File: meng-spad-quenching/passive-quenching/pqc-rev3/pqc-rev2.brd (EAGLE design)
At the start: 38.1 x 25.4 mm, 62 parts, among them IC1 OPA858, IC2 OPA858, IC3 NUD3160DMT1G, IC4 TPS7A4901, X1 CONN_SPAD, X2 VIN_PWR, X4 VIN_BIAS, X5 SIGNAL_OUT

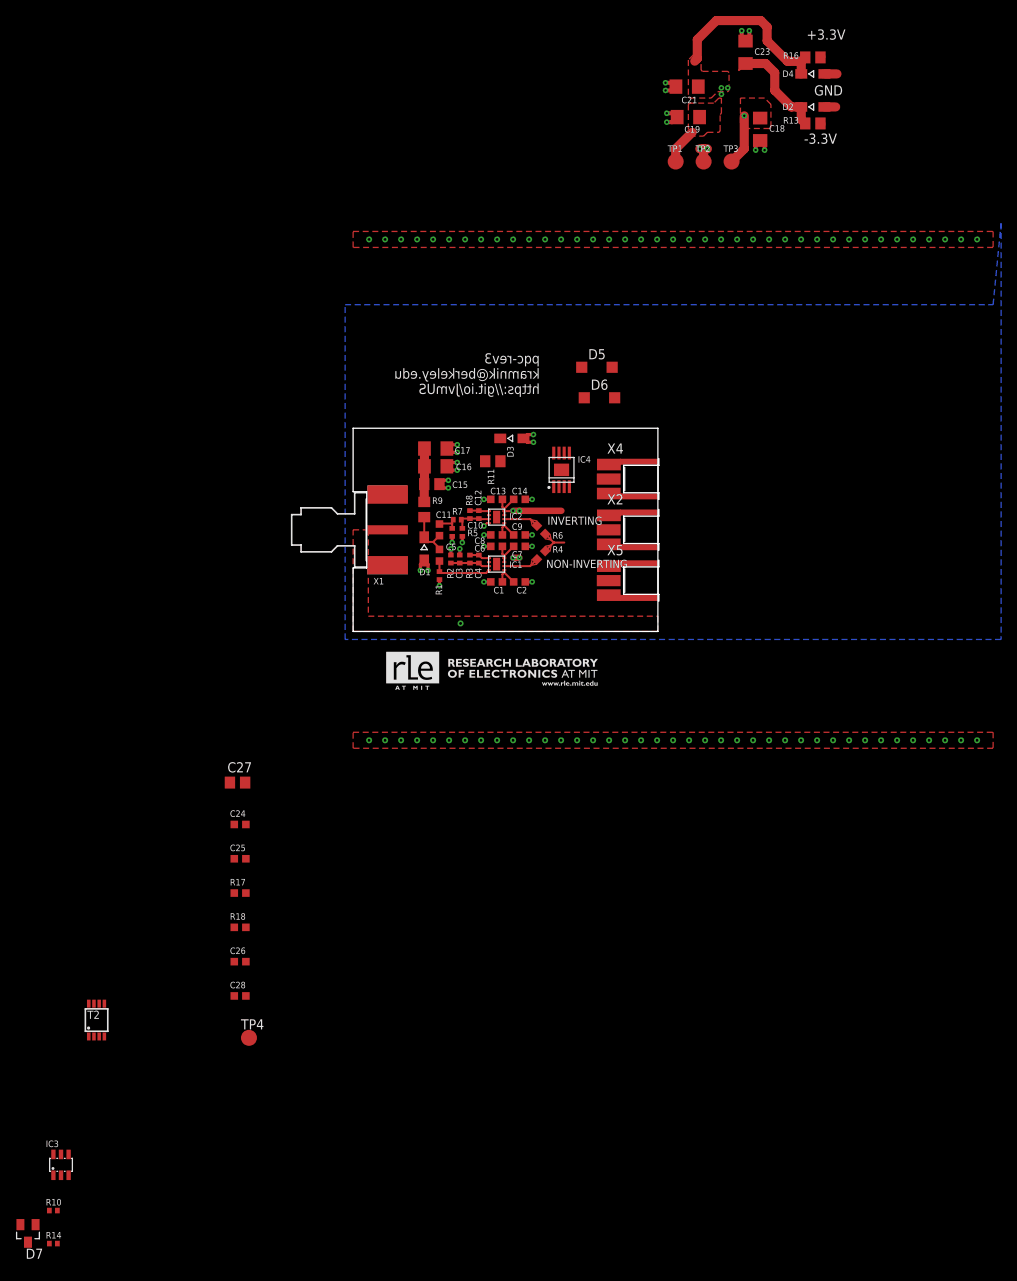
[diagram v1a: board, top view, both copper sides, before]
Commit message: 2 different power supply switching options investigated in sim
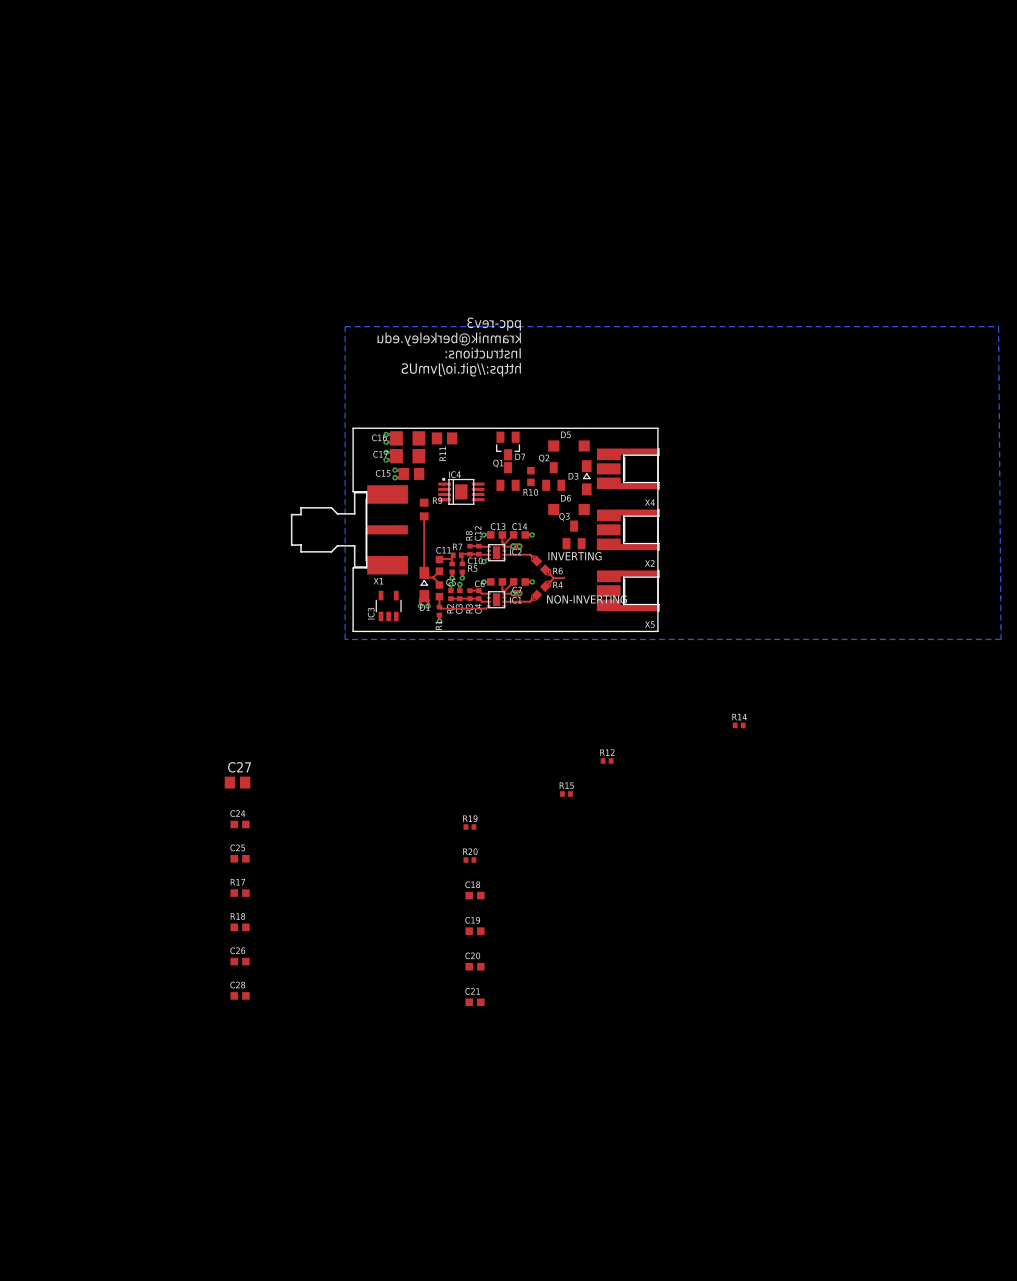
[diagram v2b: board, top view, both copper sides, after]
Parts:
- removed C1, C8: CAP CER 10000PF 25V C0G 0603, rcl-modified-footprints:C0603
- removed C2, C9: CAP CER 0.1UF 25V X7R 0603, rcl-modified-footprints:C0603
- removed C23: CAP CER 10UF 16V X7R 1206, rcl:C1206
- removed D2, D4: DF2B36FU,H3F, diode:SOD323-W
- removed R13, R16: RES SMD 1 OHM 1% 0805, rcl-modified-footprints:R0805
- removed T2: (no value), zetex:MSOP8
- removed TP1: P2V5, testpad:TP20R
- removed TP2, TP4: GND, testpad:TP20R
- removed TP3: N2V5, testpad:TP20R
- added C20: CAP CER 0.1UF 100V X7R 0603, rcl-modified-footprints:C0603
- added Q1: NTR5105P, meng:SOT23C
- added Q2: BSS123LT1G, meng:SOT23C
- added Q3: NUD3160LT1G, meng:SOT23C
- added R12: RES SMD 10M OHM 1% 1/10W 0603, rcl-modified-footprints:R0402
- added R15: RES SMD 10K OHM 1% 1/10W 0603, rcl-modified-footprints:R0402
- added R19, R20: RES SMD 1K OHM 1% 1/10W 0603, rcl-modified-footprints:R0402
- C18, C19, C21: value CAP CER 10UF 16V X7R 1206 -> CAP CER 0.1UF 100V X7R 0603; device rcl:C1206 -> rcl-modified-footprints:C0603
- C28: value CAP CER 0.1UF 25V X7R 0603 10% -> CAP CER 0.1UF 100V X7R 0603
- IC3: value NUD3160DMT1G -> LM8261; device meng:SOT23-6L -> meng:SOT23-5
- R10: value RES SMD 33K OHM 1% 1/10W 0603 -> RES SMD 10M OHM 1% 1/10W 0603; device rcl-modified-footprints:R0402 -> rcl-modified-footprints:R0603
- R14: value RES SMD 33K OHM 1% 1/10W 0603 -> RES SMD 10K OHM 1% 1/10W 0603
- R9: device rcl:R0805 -> rcl:R0603
- moved C21 117.5 mm to (15.2, -46.4), turned to 0 degrees
- moved D7 115.3 mm to (19.4, 23.2)
- moved R10 109.5 mm to (22.2, 19.4), turned to 90 degrees
- moved R14 107.4 mm to (48.3, -11.7)
- moved C19 105.2 mm to (15.2, -37.5), turned to 0 degrees
- moved C18 102.2 mm to (15.2, -33.0), turned to 0 degrees
- moved IC3 81.0 mm to (4.45, 3.17)
- moved D6 14.5 mm to (27.0, 15.2)
- moved IC4 13.7 mm to (11.4, 18.4), turned to 270 degrees
- moved D3 10.6 mm to (29.2, 19.2), turned to 270 degrees
- moved D5 10.4 mm to (27.0, 23.2)
- moved R11 6.68 mm to (11.4, 24.1)
- moved C16 4.94 mm to (6.83, 24.1), turned to 180 degrees
- moved C13 4.45 mm to (17.9, 12.1)
- moved C14 4.45 mm to (20.8, 12.1)
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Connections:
- removed net N$14: D6.A, IC3.2, X2.1
- removed net N$15: IC3.4, R14.2
- removed net N$9: IC3.5, IC3.6, R10.1
- removed net PP_N2V5_ANALOG: C1.1, C18.1, C2.1, C8.1, C9.1, TP3.TP
- removed net PP_NVIN: C23.1, D2.C, R13.1
- removed net PP_NVIN_CONN: R13.2
- removed net PP_P15V0_ANALOG: C28.1, D6.C, IC4.5, IC4.8, T2.5, T2.6
- removed net PP_P2V5_ANALOG: C19.1, TP1.TP
- removed net PP_PVIN: C21.1, D4.C, R16.1
- removed net PP_PVIN_CONN: R16.2
- new net LDO_IN: C28.1, D6.C, IC4.5, IC4.8, Q1.3
- new net LOAD_SW_NMOS_DRAIN: Q2.3, R15.1
- new net LOAD_SW_NMOS_GATE: Q2.1, Q3.3, R10.1
- new net LOAD_SW_NMOS_SOURCE: Q2.2, R14.2
- new net N$17: C18.1, IC3.3, R19.1, R20.2
- new net VPWR_IN: D6.A, Q3.1, X2.1
- new net VREF_2V5: C10.2, C20.1, C21.1, C3.2, IC3.1, IC3.4, R1.1, R2.2, R5.1
- net GND: now also C20.2, IC3.2, Q3.2, R20.1; no longer C1.2, C10.2, C2.2, C23.2, C3.2, C8.2, C9.2, D2.A, D4.A, IC3.1, R1.1, R2.2, R5.1, TP2.TP
- net LOAD_SW_PMOS_GATE: now also Q1.1, R12.1, R15.2; no longer IC3.3, T2.4
- net LOAD_SW_PMOS_SOURCE: now also Q1.2, R12.2; no longer T2.3
- net PP_P5V0_ANALOG: now also C19.1, IC3.5, R19.2; no longer TP4.TP
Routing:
- net GND: track 44.0 -> 16.1 mm, vias 116 -> 13
- net PP_PVIN: track 22.2 -> 0.00 mm
- net PP_NVIN: track 14.0 -> 0.00 mm
- net PP_N2V5_ANALOG: track 12.3 -> 0.00 mm, vias 1 -> 0
- net N$1: track 6.72 -> 0.00 mm
- net N$2: track 6.61 -> 11.2 mm
- net PP_P2V5_ANALOG: track 4.51 -> 0.00 mm
- net PP_P5V0_ANALOG: track 24.0 -> 19.8 mm
- net VREF_2V5: track 0.00 -> 3.85 mm, vias 0 -> 5
- removed copper zone on layer 1, net GND
- removed copper zone on layer 1, net PP_N2V5_ANALOG
- removed copper zone on layer 1, net PP_P2V5_ANALOG
- removed copper zone on layer 1, net PP_PVIN
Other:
- board text added: "pqc-rev3 kramnik@berkeley.edu Instructions: https://git.io/JvmUS"
- board text removed: "+3.3V"
- board text removed: "-3.3V"
- board text removed: "GND"
- board text removed: "pqc-rev3 kramnik@berkeley.edu https://git.io/JvmUS"

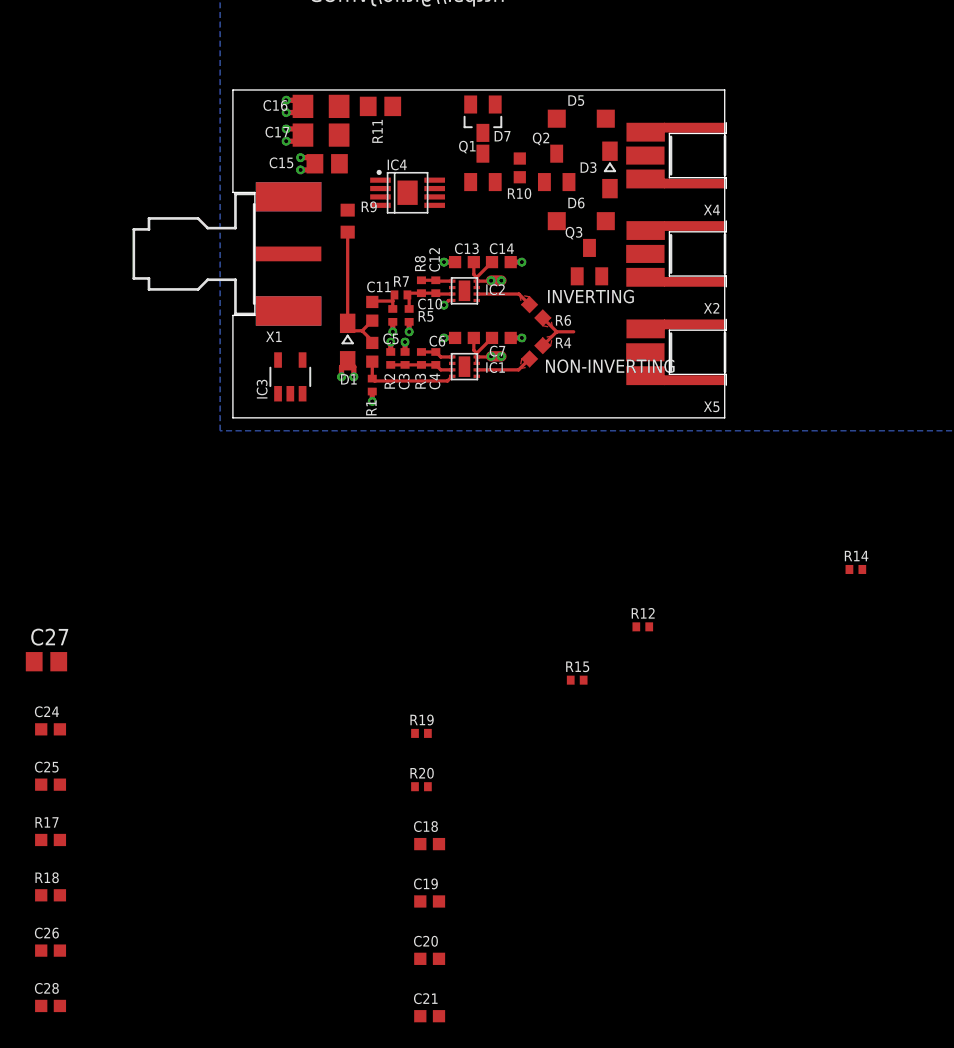
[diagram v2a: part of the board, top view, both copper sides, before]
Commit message: Everything fits on board, placement still preliminary
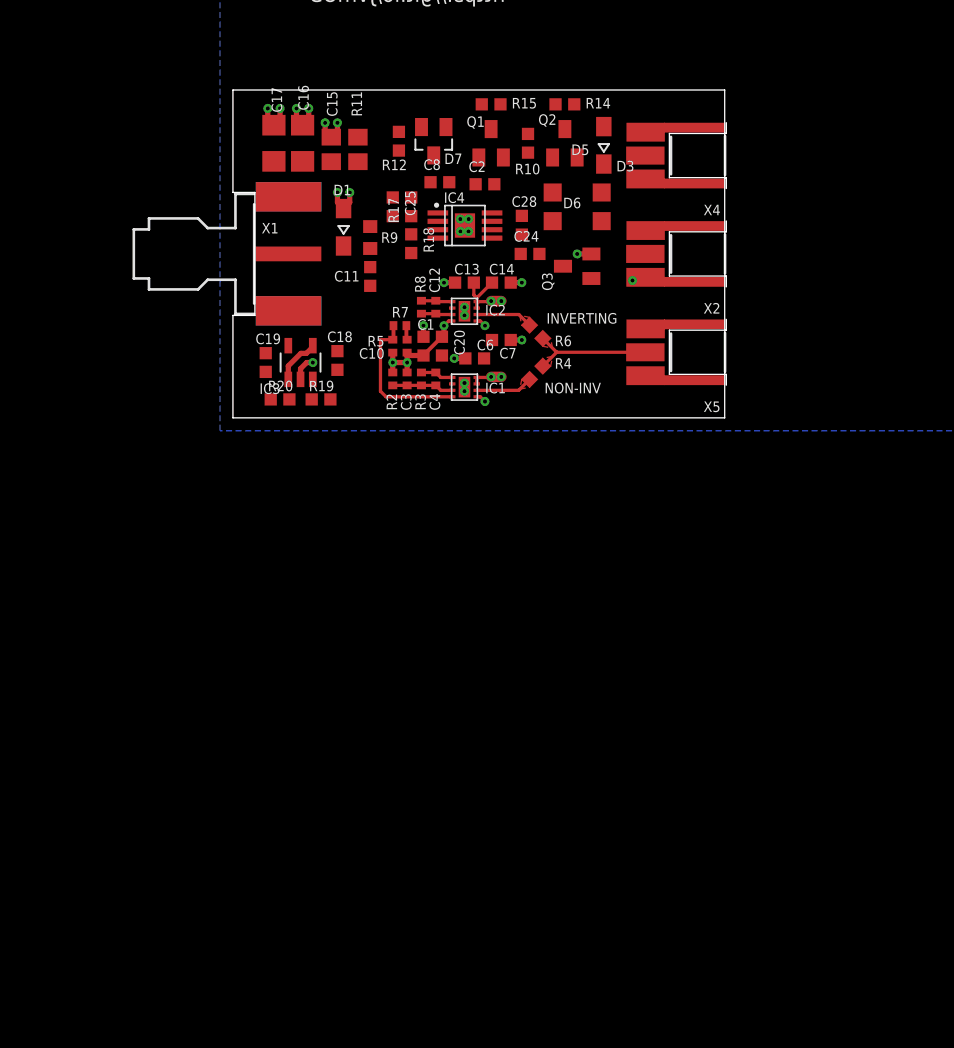
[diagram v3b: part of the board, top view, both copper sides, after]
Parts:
- removed C21: CAP CER 0.1UF 100V X7R 0603, rcl-modified-footprints:C0603
- removed C26: CAP CER 0.1UF 25V X7R 0603 10%, rcl-modified-footprints:C0603
- removed C27: CAP CER 10UF 16V X7R 0805 20%, rcl:C0805
- removed C5: C_SNS, rcl-modified-footprints:C0603
- removed R1: R_SNS, rcl-modified-footprints:R0402
- added C1: CAP CER 10000PF 25V C0G 0603, rcl-modified-footprints:C0603
- added C2: CAP CER 0.1UF 100V X7R 0603, rcl-modified-footprints:C0603
- added C8: CAP CER 10UF 10V X5R 0603, rcl-modified-footprints:C0603
- R12, R14, R15, R19, R20: device rcl-modified-footprints:R0402 -> rcl-modified-footprints:R0603
- R5: value R_SNS2 -> R_SNS
- moved C28 70.7 mm to (22.4, 14.9), turned to 90 degrees
- moved R18 57.7 mm to (13.8, 13.5), turned to 270 degrees
- moved R17 56.5 mm to (13.8, 16.4), turned to 90 degrees
- moved C24 52.3 mm to (23.0, 12.7)
- moved C25 52.0 mm to (12.4, 16.4), turned to 270 degrees
- moved C20 47.5 mm to (16.2, 5.56), turned to 270 degrees
- moved R15 45.1 mm to (20.0, 24.3), turned to 180 degrees
- moved C19 43.6 mm to (2.54, 4.29), turned to 270 degrees
- moved R14 42.5 mm to (25.7, 24.3)
- moved R12 42.1 mm to (12.9, 21.4), turned to 270 degrees
- moved C18 38.1 mm to (8.10, 4.45), turned to 90 degrees
- moved R20 31.9 mm to (3.65, 1.43)
- moved R19 27.0 mm to (6.83, 1.43)
- moved D1 8.90 mm to (8.57, 14.8), turned to 90 degrees
- moved D5 5.72 mm to (26.7, 17.5)
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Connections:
- net LDO_P5V0_FB_CH1 renamed LDO_FB
- net N$17 renamed VREF_DIVIDER
- removed net N$3: C11.2, R5.2, R7.2
- net GND: now also C1.2, C2.2, C8.2; no longer C21.2, C26.2, C27.2, IC2.4
- net N$2: no longer C5.1
- net N$6: now also C11.2, R5.2, R7.2; no longer C5.2, R1.2
- net PP_P5V0_ANALOG: now also C2.1, C8.1; no longer C26.1, C27.1
- net VREF_2V5: now also C1.1, IC2.4; no longer C21.1, R1.1
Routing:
- net N$2: track 11.2 -> 0.59 mm
- net PP_P5V0_ANALOG: track 19.8 -> 9.68 mm
- net VREF_2V5: track 3.85 -> 12.9 mm, vias 5 -> 3
- net N$12: track 4.36 -> 9.91 mm
- net GND: track 16.1 -> 20.9 mm, vias 13 -> 26
- net N$6: track 7.73 -> 11.8 mm
- net N$3: track 2.76 -> 0.00 mm
- net N$4: track 4.70 -> 3.51 mm
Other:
- board text added: "NON-INV"
- board text removed: "NON-INVERTING"
